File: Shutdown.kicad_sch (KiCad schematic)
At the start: 44 parts, among them J1 0194270049, J2 0194270031, Q1 SI2347DS-T1-GE3, Q2 SI2347DS-T1-GE3, Q4 SI2318CDS-T1-GE3, Q5 SI2318CDS-T1-GE3, Q6 SI2318CDS-T1-GE3, Q7 SI2347DS-T1-GE3

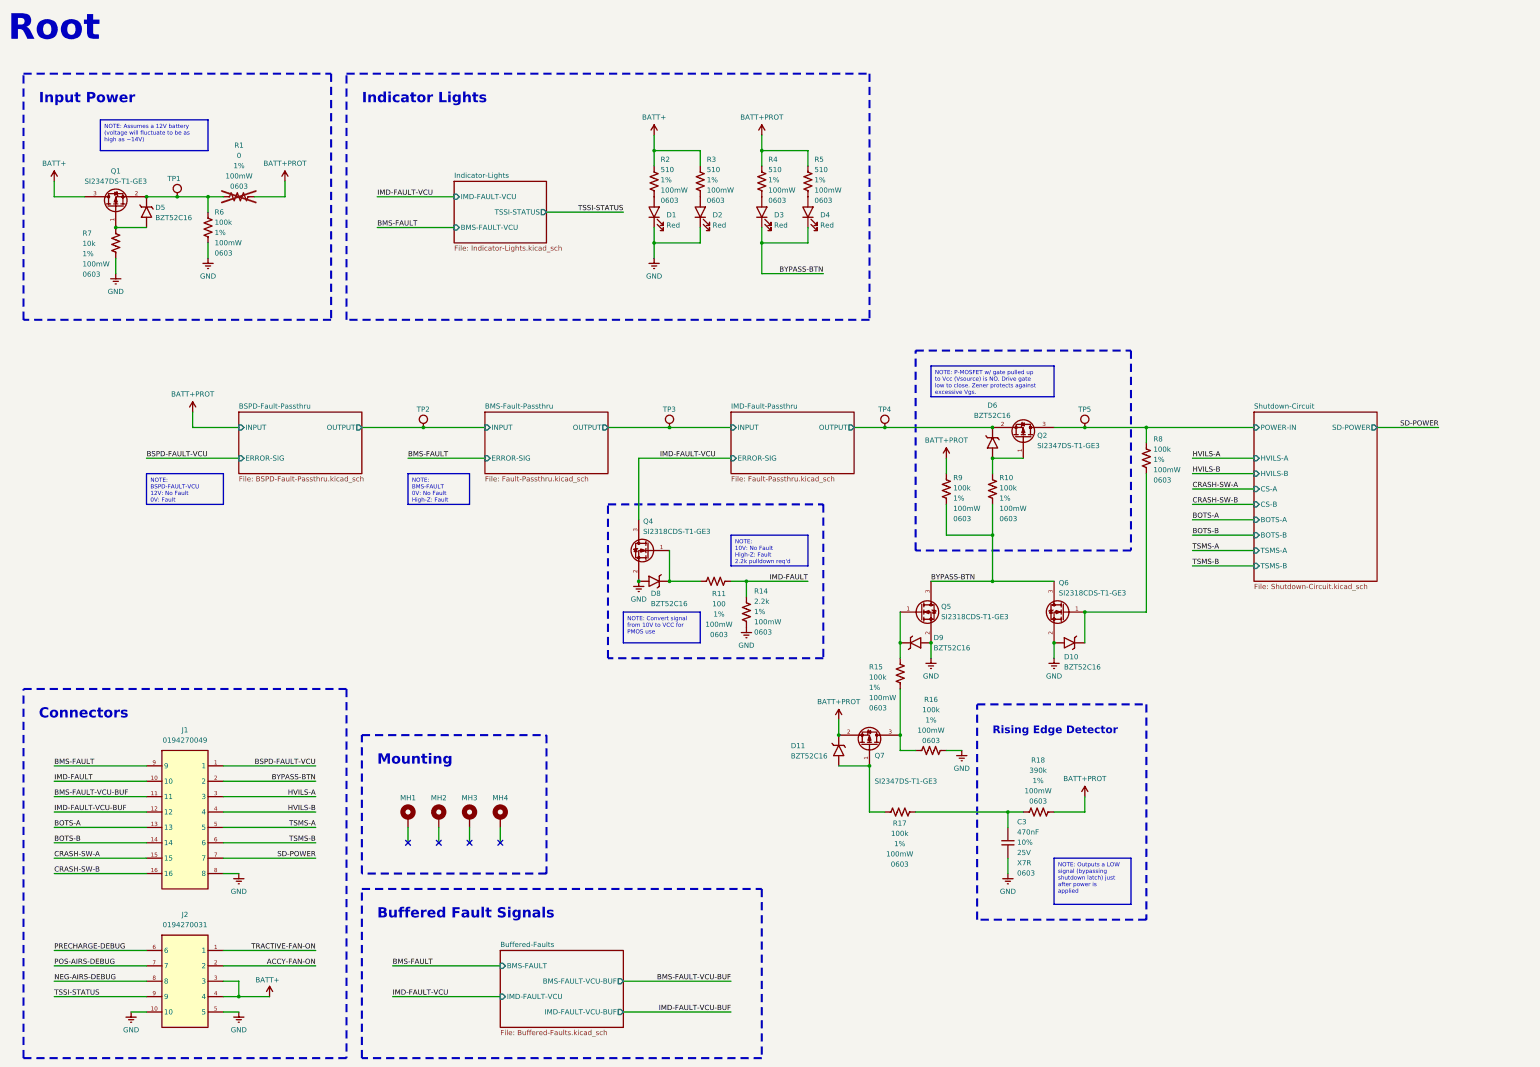
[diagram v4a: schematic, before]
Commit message: Schem is reannotated time to redo all of the layout
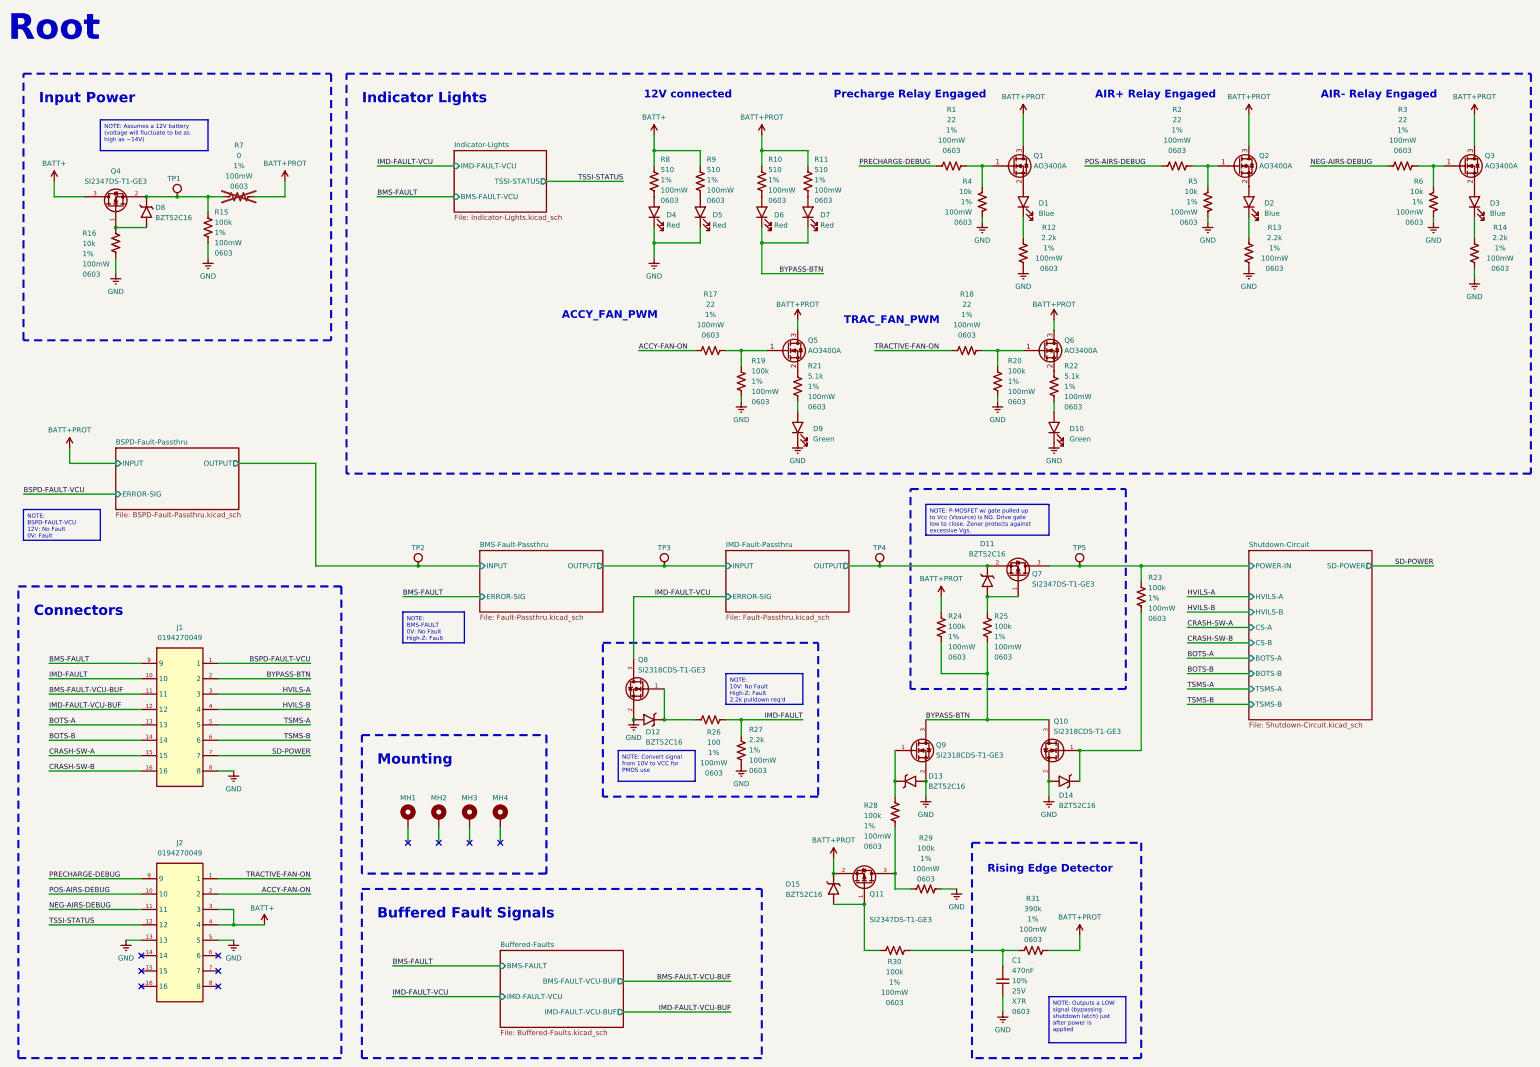
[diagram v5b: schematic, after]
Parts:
- removed J2: 0194270031, -Connectors:0194270031, symbol -Connectors:0194270031
- added D1, D2, D3: Blue, LED_SMD:LED_0805_2012Metric, symbol -Diodes-LED:NCD0805B2
- added D10, D9: Green, LED_SMD:LED_0805_2012Metric, symbol -Diodes-LED:NCD0805G1
- added J2: 0194270049, -Connectors:0194270049, symbol -Connectors:0194270049
- added Q1, Q2, Q3, Q5, Q6: AO3400A, Package_TO_SOT_SMD:SOT-23, symbol Transistor_FET:AO3400A
- added R1, R17, R18, R2, R3: 22, Resistor_SMD:R_0603_1608Metric_Pad0.98x0.95mm_HandSolder, symbol -R-SMD-0603:R-0603-22-1%-100mW-100PPM_1
- added R12, R13, R14: 2.2k, Resistor_SMD:R_0603_1608Metric_Pad0.98x0.95mm_HandSolder, symbol -R-SMD-0603:R-0603-2.2k-1%-100mW-100PPM
- added R19, R20: 100k, Resistor_SMD:R_0603_1608Metric_Pad0.98x0.95mm_HandSolder, symbol -R-SMD-0603:R-0603-100k-1%-100mW-100PPM
- added R21, R22: 5.1k, Resistor_SMD:R_0603_1608Metric_Pad0.98x0.95mm_HandSolder, symbol -R-SMD-0603:R-0603-5.1k-1%-100mW-100PPM_1_1
- added R4, R5, R6: 10k, Resistor_SMD:R_0603_1608Metric_Pad0.98x0.95mm_HandSolder, symbol -R-SMD-0603:R-0603-10k-1%-100mW-100PPM
- renumbered C3 to C1, D6 to D11, D8 to D12, D9 to D13, D10 to D14, D11 to D15, D1 to D4, D2 to D5, D3 to D6, D4 to D7, D5 to D8, Q6 to Q10, Q7 to Q11, Q1 to Q4, Q2 to Q7, Q4 to Q8, Q5 to Q9, R4 to R10, R5 to R11, R6 to R15, R7 to R16, R8 to R23, R9 to R24, R10 to R25, R11 to R26, R14 to R27, R15 to R28, R16 to R29, R17 to R30, R18 to R31, R1 to R7, R2 to R8, R3 to R9
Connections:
- net ACCY-FAN-ON: now also J2.2, R17.1
- net BATT+: now also J2.3, J2.4
- net BATT+PROT: now also Q1.3 (D), Q2.3 (D), Q3.3 (D), Q5.3 (D), Q6.3 (D)
- net GND: now also D10.1 (K), D9.1 (K), J2.13, J2.5, R12.2, R13.2, R14.2, R19.1, R20.1, R4.2, R5.2, R6.2
- net NEG-AIRS-DEBUG: now also J2.11, R3.1
- net POS-AIRS-DEBUG: now also J2.10, R2.1
- net PRECHARGE-DEBUG: now also J2.9, R1.1
- net TRACTIVE-FAN-ON: now also J2.1, R18.1
- net TSSI-STATUS: now also J2.12
- new net: D1.1 (K), R12.1
- new net: D1.2 (A), Q1.2 (S)
- new net: D2.1 (K), R13.1
- new net: D10.2 (A), R22.1
- new net: Q2.1 (G), R2.2, R5.1
- new net: D2.2 (A), Q2.2 (S)
- new net: D9.2 (A), R21.1
- new net: Q6.1 (G), R18.2, R20.2
- new net: Q1.1 (G), R1.2, R4.1
- new net: Q6.2 (S), R22.2
- new net: D3.1 (K), R14.1
- new net: D3.2 (A), Q3.2 (S)
- new net: Q5.2 (S), R21.2
- new net: Q3.1 (G), R3.2, R6.1
- new net: Q5.1 (G), R17.2, R19.2
- no-connect marks 4 -> 10
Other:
- note added: "12V connected"
- note added: "ACCY_FAN_PWM"
- note added: "AIR+ Relay Engaged"
- note added: "AIR- Relay Engaged"
- note added: "Precharge Relay Engaged"
- note added: "TRAC_FAN_PWM"
- moved on the sheet: C1, D11, D12, D13, D14, D15, J1, Q10, Q11, Q7, Q8, Q9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

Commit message: Finished shutdown, 0 drc, need to export gerbers
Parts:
- added D10, D2, D8: Blue, LED_SMD:LED_0805_2012Metric, symbol -Diodes-LED:NCD0805B2
- added D13, D15: Green, LED_SMD:LED_0805_2012Metric, symbol -Diodes-LED:NCD0805G1
- added R14, R16, R18: 2.2k, Resistor_SMD:R_0603_1608Metric_Pad0.98x0.95mm_HandSolder, symbol -R-SMD-0603:R-0603-2.2k-1%-100mW-100PPM
- added R25, R27: 5.1k, Resistor_SMD:R_0603_1608Metric_Pad0.98x0.95mm_HandSolder, symbol -R-SMD-0603:R-0603-5.1k-1%-100mW-100PPM_1_1
- renumbered TP3 to BMS1, TP2 to BSPD1, TP5 to BYPASS1, D8 to D11, D9 to D12, D10 to D14, D11 to D16, D12 to D17, D13 to D18, D14 to D19, D15 to D20, D4 to D3, D5 to D4, D6 to D5, D7 to D6, D2 to D7, D3 to D9, TP4 to IMD1, R15 to R12, R12 to R13, R13 to R15, R14 to R17, R16 to R19, R17 to R20, R18 to R21, R19 to R22, R20 to R23, R21 to R24, R22 to R26, R23 to R28, R24 to R29, R25 to R30, R26 to R31, R27 to R32, R28 to R33, R29 to R34, R30 to R35, R31 to R36, TP1 to VIN1
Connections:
- net GND: now also D13.1 (K), D15.1 (K), R14.2, R16.2, R18.2
- net at D1.2 (A), Q1.2 (S): now also D2.2 (A)
- net at D7.2 (A), Q2.2 (S): now also D8.2 (A)
- net at Q6.2 (S), R26.2: now also R27.2
- net at D9.2 (A), Q3.2 (S): now also D10.2 (A)
- net at Q5.2 (S), R24.2: now also R25.2
- new net: D13.2 (A), R25.1
- new net: D8.1 (K), R16.1
- new net: D2.1 (K), R14.1
- new net: D10.1 (K), R18.1
- new net: D15.2 (A), R27.1
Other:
- moved on the sheet: D1, D12, D14, D7, D9, R13, R15, R17, R24, R26

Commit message: added comments to add that for future revs there should be a pulldown between shutdown fault passthru stages
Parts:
- BMS1, BSPD1, BYPASS1, IMD1, MH1, MH2, MH3, MH4, VIN1: value ~ -> (none)

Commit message: schematic updated to V2 extra crispy
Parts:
- removed D1, D10, D2, D7, D8, D9: Blue, LED_SMD:LED_0805_2012Metric, symbol -Diodes-LED:NCD0805B2
- removed D12, D13, D14, D15: Green, LED_SMD:LED_0805_2012Metric, symbol -Diodes-LED:NCD0805G1
- removed D3, D4, D5, D6: Red, LED_SMD:LED_0805_2012Metric, symbol -Diodes-LED:NCD0805R1
- removed Q1, Q2, Q3, Q5, Q6: AO3400A, Package_TO_SOT_SMD:SOT-23, symbol Transistor_FET:AO3400A
- removed Q11: SI2347DS-T1-GE3, Package_TO_SOT_SMD:SOT-23-3, symbol -MOSFET-P-Channel:SI2347DS-T1-GE3
- removed R1, R2, R20, R21, R3: 22, Resistor_SMD:R_0603_1608Metric_Pad0.98x0.95mm_HandSolder, symbol -R-SMD-0603:R-0603-22-1%-100mW-100PPM_1
- removed R10, R11, R8, R9: 510, Resistor_SMD:R_0603_1608Metric_Pad0.98x0.95mm_HandSolder, symbol -R-SMD-0603:R-0603-510-1%-100mW-100PPM
- removed R13, R14, R15, R16, R17, R18, R32: 2.2k, Resistor_SMD:R_0603_1608Metric_Pad0.98x0.95mm_HandSolder, symbol -R-SMD-0603:R-0603-2.2k-1%-100mW-100PPM
- removed R22, R23: 100k, Resistor_SMD:R_0603_1608Metric_Pad0.98x0.95mm_HandSolder, symbol -R-SMD-0603:R-0603-100k-1%-100mW-100PPM
- removed R24, R25, R26, R27: 5.1k, Resistor_SMD:R_0603_1608Metric_Pad0.98x0.95mm_HandSolder, symbol -R-SMD-0603:R-0603-5.1k-1%-100mW-100PPM_1_1
- removed R4, R5, R6: 10k, Resistor_SMD:R_0603_1608Metric_Pad0.98x0.95mm_HandSolder, symbol -R-SMD-0603:R-0603-10k-1%-100mW-100PPM
- added Q6: SI2347DS-T1-GE3, Package_TO_SOT_SMD:SOT-23-3, symbol -MOSFET-P-Channel:SI2347DS-T1-GE3
- added R8: 2.2k, Resistor_SMD:R_2512_6332Metric_Pad1.40x3.35mm_HandSolder, symbol -R-SMD-2512:R-2512-2.2k-5%-1W-100PPM
- MH1, MH2, MH3, MH4: Fastener (none) -> M3
- renumbered D11 to D1, D16 to D2, D17 to D3, D18 to D4, D19 to D5, D20 to D6, Q4 to Q1, Q7 to Q2, Q8 to Q3, Q9 to Q4, Q10 to Q5, R7 to R1, R34 to R10, R35 to R11, R36 to R12, R12 to R2, R19 to R3, R28 to R4, R29 to R5, R30 to R6, R31 to R7, R33 to R9
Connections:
- net BATT+PROT: now also Q6.2 (S)
- net GND: now also R8.1
- net IMD-FAULT: now also R8.2
- net at R10.1, R9.1: now also Q6.3 (D)
- net at D6.2 (A), R11.1: now also Q6.1 (G)
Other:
- sheet Indicator-Lights renamed TSSI-Status-Signal
- added sheet Debug-Lights (Debug-Lights.kicad_sch)
- sheet TSSI-Status-Signal: file Indicator-Lights.kicad_sch -> TSSI-Status-Signal.kicad_sch
- note added: "Debug Lights"
- note added: "TSSI Status Signal"
- note removed: "12V connected"
- note removed: "ACCY_FAN_PWM"
- note removed: "AIR+ Relay Engaged"
- note removed: "AIR- Relay Engaged"
- note removed: "Indicator Lights"
- note removed: "Precharge Relay Engaged"
- note removed: "TRAC_FAN_PWM"
- moved on the sheet: C1, D2, D3, D4, D5, D6, J1, J2, Q2, Q3, Q4, Q5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
